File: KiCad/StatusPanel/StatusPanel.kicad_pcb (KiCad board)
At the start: 2 copper layers, 95 x 85 mm, 17 parts, among them U1 CC56-12EWA

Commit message: ステータスパネルの3Dモデルを生成
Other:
- board text removed: "N2O"
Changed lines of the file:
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@@
       (stroke (width 0.05) (type solid)) (fill none) (layer "F.CrtYd"))
     (pad "" np_thru_hole circle (at 0 0) (size 7 7) (drill 7) (layers "F&B.Cu" "*.Mask"))
+    (model "${KIPRJMOD}/LED_Bracket_Red.step"
+      (offset (xyz 0 0 0))
+      (scale (xyz 1 1 1))
+      (rotate (xyz 0 0 0))
+    )
   )
   (footprint "MountingHole:MountingHole_4.5mm" (layer "F.Cu")
@@
       (stroke (width 0.05) (type solid)) (fill none) (layer "F.CrtYd"))
     (pad "" np_thru_hole circle (at 0 0) (size 7 7) (drill 7) (layers "*.Cu" "*.Mask"))
+    (model "${KIPRJMOD}/LED_Bracket_Red.step"
+      (offset (xyz 0 0 0))
+      (scale (xyz 1 1 1))
+      (rotate (xyz 0 0 0))
+    )
   )
   (footprint "MountingHole:MountingHole_4.5mm" (layer "F.Cu")
@@
       (stroke (width 0.05) (type solid)) (fill none) (layer "F.CrtYd"))
     (pad "" np_thru_hole circle (at 0 0) (size 7 7) (drill 7) (layers "*.Cu" "*.Mask"))
+    (model "${KIPRJMOD}/LED_Bracket_Green.step"
+      (offset (xyz 0 0 0))
+      (scale (xyz 1 1 1))
+      (rotate (xyz 0 0 0))
+    )
   )
   (footprint "MountingHole:MountingHole_6mm" (layer "F.Cu")
@@
       (stroke (width 0.05) (type solid)) (fill none) (layer "F.CrtYd"))
     (pad "" np_thru_hole circle (at 0 0) (size 7 7) (drill 7) (layers "*.Cu" "*.Mask"))
+    (model "${KIPRJMOD}/LED_Bracket_Orange.step"
+      (offset (xyz 0 0 0))
+      (scale (xyz 1 1 1))
+      (rotate (xyz 0 0 0))
+    )
   )
   (footprint "MountingHole:MountingHole_6mm" (layer "F.Cu")
@@
       (stroke (width 0.05) (type solid)) (fill none) (layer "F.CrtYd"))
     (pad "" np_thru_hole circle (at 0 0) (size 22 22) (drill 22) (layers "F&B.Cu" "*.Mask"))
+    (model "${KIPRJMOD}/USB.step"
+      (offset (xyz 0 0 0))
+      (scale (xyz 1 1 1))
+      (rotate (xyz 0 0 0))
+    )
   )
   (footprint "MountingHole:MountingHole_6mm" (layer "F.Cu")
@@
       (stroke (width 0.05) (type solid)) (fill none) (layer "F.CrtYd"))
     (pad "" np_thru_hole circle (at 0 0) (size 7 7) (drill 7) (layers "*.Cu" "*.Mask"))
+    (model "${KIPRJMOD}/LED_Bracket_Green.step"
+      (offset (xyz 0 0 0))
+      (scale (xyz 1 1 1))
+      (rotate (xyz 0 0 0))
+    )
   )
   (footprint "MountingHole:MountingHole_4.5mm" (layer "F.Cu")
@@
       (stroke (width 0.05) (type solid)) (fill none) (layer "F.CrtYd"))
     (pad "" np_thru_hole circle (at 0 0) (size 7 7) (drill 7) (layers "*.Cu" "*.Mask"))
+    (model "${KIPRJMOD}/LED_Bracket_Orange.step"
+      (offset (xyz 0 0 0))
+      (scale (xyz 1 1 1))
+      (rotate (xyz 0 0 0))
+    )
   )
   (footprint "MountingHole:MountingHole_6mm" (layer "F.Cu")
@@
       (stroke (width 0.05) (type solid)) (fill none) (layer "F.CrtYd"))
     (pad "" np_thru_hole circle (at 0 0) (size 7 7) (drill 7) (layers "*.Cu" "*.Mask"))
+    (model "${KIPRJMOD}/LED_Bracket_Blue.step"
+      (offset (xyz 0 0 0))
+      (scale (xyz 1 1 1))
+      (rotate (xyz 0 0 0))
+    )
   )
   (footprint "MountingHole:MountingHole_4.5mm" (layer "F.Cu")
@@
       (stroke (width 0.05) (type solid)) (fill none) (layer "F.CrtYd"))
     (pad "" np_thru_hole circle (at 0 0) (size 13.77 13.77) (drill 13.77) (layers "F&B.Cu" "*.Mask"))
+    (model "${KIPRJMOD}/Button.step"
+      (offset (xyz 0 0 0))
+      (scale (xyz 1 1 1))
+      (rotate (xyz 0 0 0))
+    )
   )
   (footprint "MountingHole:MountingHole_4.5mm" (layer "F.Cu")
@@
       (stroke (width 0.05) (type solid)) (fill none) (layer "F.CrtYd"))
     (pad "" np_thru_hole circle (at 0 0) (size 7 7) (drill 7) (layers "*.Cu" "*.Mask"))
+    (model "${KIPRJMOD}/LED_Bracket_Blue.step"
+      (offset (xyz 0 0 0))
+      (scale (xyz 1 1 1))
+      (rotate (xyz 0 0 0))
+    )
   )
   (footprint "Display_7Segment:CA56-12CGKWA" (layer "F.Cu")
@@
     (effects (font (size 2 2) (thickness 0.3)) (justify top))
   )
-  (gr_text "N2O" (at 123.85 58.9) (layer "F.SilkS")
-    (effects (font (size 3 3) (thickness 0.3)) (justify left))
-  )
   (gr_text "SYSTEM" (at 85.85 91.9) (layer "F.SilkS")
     (effects (font (size 2 2) (thickness 0.3)))
@@
     (effects (font (size 2 2) (thickness 0.3)) (justify top))
   )
-  (gr_text "MPa" (at 122.85 66.9) (layer "F.SilkS")
-    (effects (font (size 7 7) (thickness 0.5)) (justify left))
+  (gr_text "MPa" (at 121.85 63.9) (layer "F.SilkS")
+    (effects (font (size 7 7) (thickness 0.7)) (justify left))
   )
   (gr_text "RESET" (at 104.85 116.9) (layer "F.SilkS")

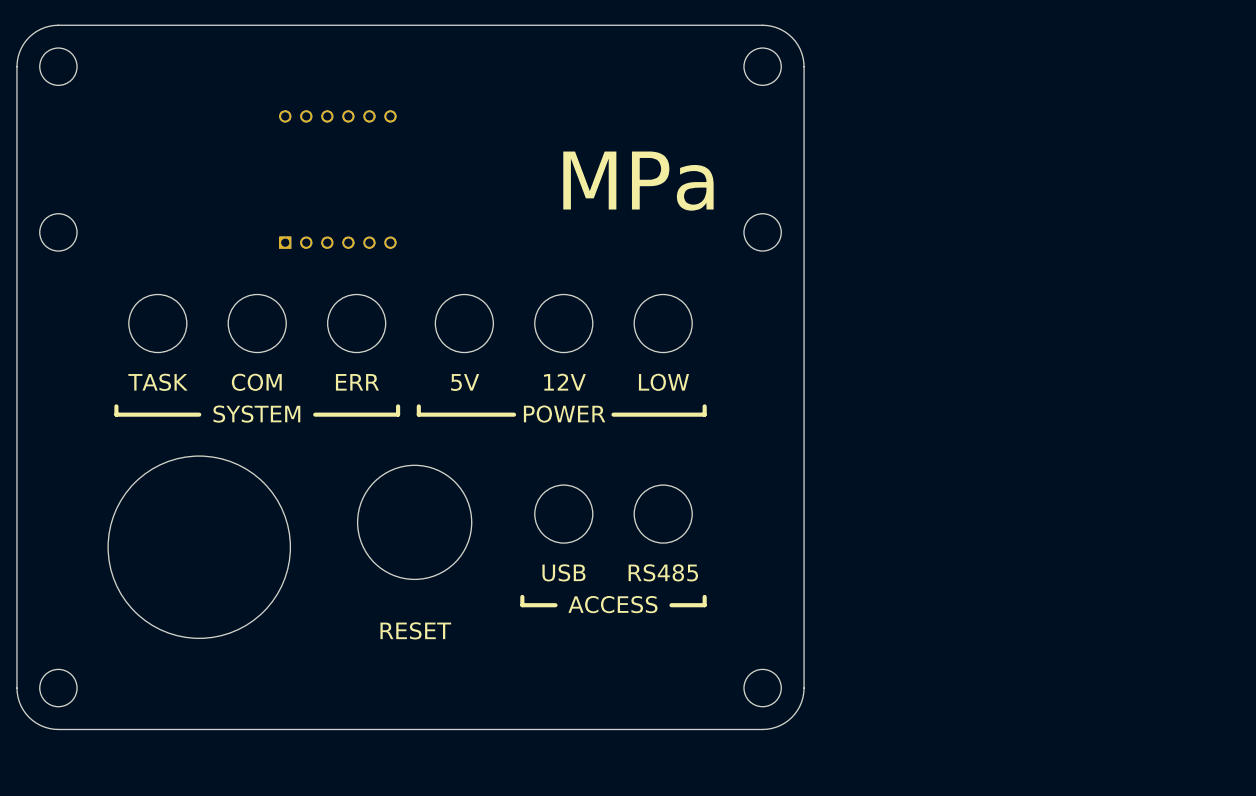
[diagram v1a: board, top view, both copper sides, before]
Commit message: ステータスパネルを再設計
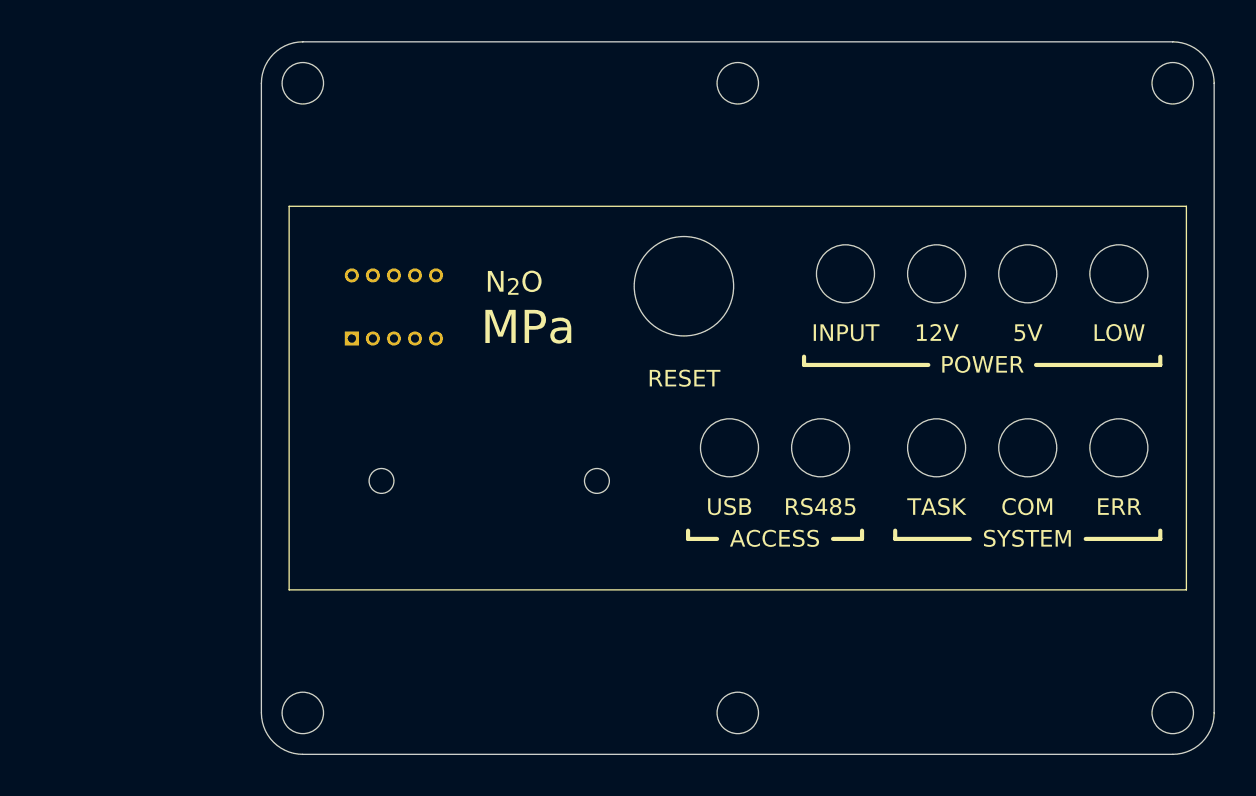
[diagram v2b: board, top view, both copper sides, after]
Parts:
- removed the REF** at (146.8, 69.9)
- removed the REF** at (61.9, 124.9)
- removed the REF** at (61.9, 49.9)
- removed the REF** at (146.8, 49.9)
- removed the REF** at (146.8, 124.9)
- removed the REF** at (61.9, 69.9)
- removed U1: CC56-12EWA, Display_7Segment:CA56-12CGKWA
- added REF**: MountingHole_5mm, MountingHole:MountingHole_5mm, F.Cu at (91.3, 51.9)
- added REF**: MountingHole_6mm, MountingHole:MountingHole_6mm, F.Cu at (156.8, 74.9)
- added REF**: MountingHole_5mm, MountingHole:MountingHole_5mm, F.Cu at (143.8, 127.9)
- added REF**: MountingHole_5mm, MountingHole:MountingHole_5mm, F.Cu at (143.8, 51.9)
- added REF**: MountingHole_5mm, MountingHole:MountingHole_5mm, F.Cu at (91.3, 127.9)
- added REF**: MountingHole_5mm, MountingHole:MountingHole_5mm, F.Cu at (196.3, 51.9)
- added REF**: Sx39-1xxxxx, Display_7Segment:Sx39-1xxxxx, F.Cu at (97.3, 82.7)
- added REF**: MountingHole_5mm, MountingHole:MountingHole_5mm, F.Cu at (196.3, 127.9)
- moved REF** 95.2 mm to (167.8, 95.9)
- moved REF** 94.2 mm to (178.8, 95.9)
- moved REF** 93.2 mm to (189.8, 95.9)
- moved REF** 57.3 mm to (167.8, 74.9)
- moved REF** 56.3 mm to (178.8, 74.9)
- moved REF** 55.3 mm to (189.8, 74.9)
- moved REF** 43.2 mm to (137.3, 76.4)
- moved REF** 35.9 mm to (113.8, 99.9)
- moved REF** 21.5 mm to (142.8, 95.9)
- moved REF** 20.6 mm to (153.8, 95.9)
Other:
- board size 95 x 85 mm -> 115 x 86 mm
- board text added: "INPUT"
- board text added: "N_{2}O"
- board text removed: "LaunchController"
- board text removed: "SatelliteController"

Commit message: ステータスパネルの裏面に配線を追加
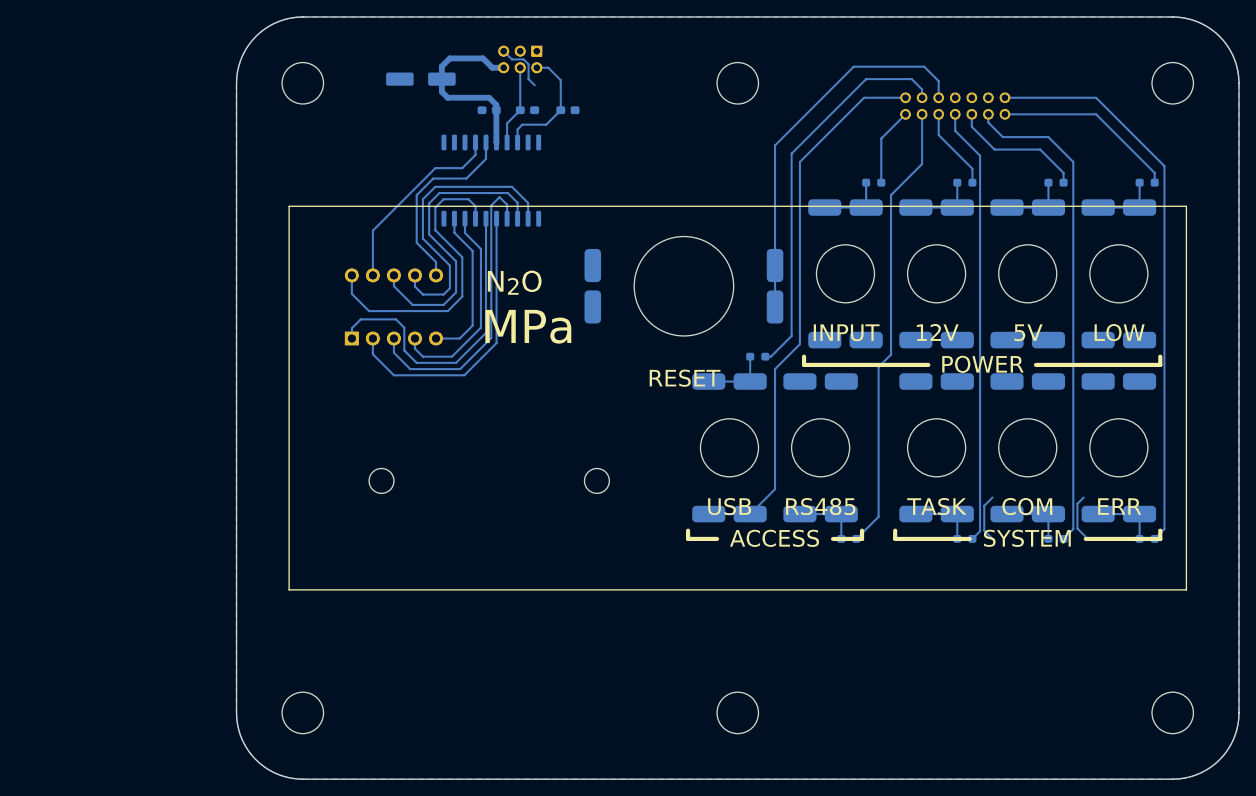
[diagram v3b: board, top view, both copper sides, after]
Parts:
- removed the REF** at (97.3, 82.7)
- added C1: 0.1uF, Capacitor_SMD:C_0603_1608Metric_Pad1.08x0.95mm_HandSolder, B.Cu at (113.8, 55.1)
- added C2: 0.1uF, Capacitor_SMD:C_0603_1608Metric_Pad1.08x0.95mm_HandSolder, B.Cu at (123.3, 55.1)
- added C3: 0.1uF, Capacitor_SMD:C_0603_1608Metric_Pad1.08x0.95mm_HandSolder, B.Cu at (118.5, 55.1)
- added C4: 100uF, Capacitor_SMD:C_Elec_6.3x7.7, B.Cu at (105.6, 51.4)
- added J1: CONN, TSRP_Connector_Hirose:DF51A-14DP-2DS, B.Cu at (164.1, 55.6)
- added J10: CONN_12V_CTL, TSRP_Connector_Generic:1p, B.Cu at (167.8, 66.9)
- added J11: CONN_12V_GND, TSRP_Connector_Generic:1p, B.Cu at (167.8, 82.9)
- added J12: CONN_TASK_CTL, TSRP_Connector_Generic:1p, B.Cu at (167.8, 103.9)
- added J13: CONN_TASK_GND, TSRP_Connector_Generic:1p, B.Cu at (167.8, 87.9)
- added J14: CONN_5V_CTL, TSRP_Connector_Generic:1p, B.Cu at (178.8, 66.9)
- added J15: CONN_5V_GND, TSRP_Connector_Generic:1p, B.Cu at (178.8, 82.9)
- added J16: CONN_COM_CTL, TSRP_Connector_Generic:1p, B.Cu at (178.8, 103.9)
- added J17: CONN_COM_GND, TSRP_Connector_Generic:1p, B.Cu at (178.8, 87.9)
- added J18: CONN_LOW_CTL, TSRP_Connector_Generic:1p, B.Cu at (189.8, 66.9)
- added J19: CONN_LOW_GND, TSRP_Connector_Generic:1p, B.Cu at (189.8, 82.9)
- added J2: CONN_RESET_CTL, TSRP_Connector_Generic:1p, B.Cu at (148.3, 76.4)
- added J20: CONN_ERROR_CTL, TSRP_Connector_Generic:1p, B.Cu at (189.8, 103.9)
- added J21: CONN_ERROR_GND, TSRP_Connector_Generic:1p, B.Cu at (189.8, 87.9)
- added J22: CONN_7SEG, TSRP_Connector_Hirose:DF51A-6DP-2DSA, B.Cu at (117.6, 49.0)
- added J3: CONN_RESET_GND, TSRP_Connector_Generic:1p, B.Cu at (126.3, 76.4)
- added J4: CONN_USB_5V, TSRP_Connector_Generic:1p, B.Cu at (142.8, 103.9)
- added J5: CONN_USB_CTL, TSRP_Connector_Generic:1p, B.Cu at (142.8, 87.9)
- added J6: CONN_INPUT_CTL, TSRP_Connector_Generic:1p, B.Cu at (156.8, 66.9)
- added J7: CONN_INPUT_GND, TSRP_Connector_Generic:1p, B.Cu at (156.8, 82.9)
- added J8: CONN_RS485_CTL, TSRP_Connector_Generic:1p, B.Cu at (153.8, 103.9)
- added J9: CONN_RS485_GND, TSRP_Connector_Generic:1p, B.Cu at (153.8, 87.9)
- added R1: R, Resistor_SMD:R_0603_1608Metric_Pad0.98x0.95mm_HandSolder, B.Cu at (146.3, 84.9)
- added R2: R, Resistor_SMD:R_0603_1608Metric_Pad0.98x0.95mm_HandSolder, B.Cu at (160.3, 63.9)
- added R3: R, Resistor_SMD:R_0603_1608Metric_Pad0.98x0.95mm_HandSolder, B.Cu at (157.3, 106.9)
- added R4: R, Resistor_SMD:R_0603_1608Metric_Pad0.98x0.95mm_HandSolder, B.Cu at (171.3, 63.9)
- added R5: R, Resistor_SMD:R_0603_1608Metric_Pad0.98x0.95mm_HandSolder, B.Cu at (171.3, 106.9)
- added R6: R, Resistor_SMD:R_0603_1608Metric_Pad0.98x0.95mm_HandSolder, B.Cu at (182.3, 63.9)
- added R7: R, Resistor_SMD:R_0603_1608Metric_Pad0.98x0.95mm_HandSolder, B.Cu at (182.3, 106.9)
- added R8: R, Resistor_SMD:R_0603_1608Metric_Pad0.98x0.95mm_HandSolder, B.Cu at (193.3, 63.9)
- added R9: R, Resistor_SMD:R_0603_1608Metric_Pad0.98x0.95mm_HandSolder, B.Cu at (193.3, 106.9)
- added U1: 2281SB, Display_7Segment:Sx39-1xxxxx, F.Cu at (97.3, 82.7)
- added U2: TM1637, Package_SO:SOP-20_7.5x12.8mm_P1.27mm, B.Cu at (114.1, 63.6)
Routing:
- net ERROR: track 0.00 -> 68.2 mm
- net +5V: track 0.00 -> 65.9 mm
- net COM: track 0.00 -> 59.2 mm
- net RS485: track 0.00 -> 54.5 mm
- net TASK: track 0.00 -> 52.9 mm
- net USB: track 0.00 -> 47.2 mm
- net RESET: track 0.00 -> 45.9 mm
- net Net-(U1-E): track 0.00 -> 36.9 mm
- net Net-(U1-F): track 0.00 -> 36.4 mm
- net Net-(U1-C): track 0.00 -> 36.2 mm
- net Net-(U1-B): track 0.00 -> 36.1 mm
- net Net-(U1-D): track 0.00 -> 34.5 mm
- net Net-(U1-A): track 0.00 -> 34.4 mm
- net Net-(U1-G): track 0.00 -> 25.0 mm
- net +5VP: track 0.00 -> 23.2 mm
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- added copper zone on B.Cu, net GND
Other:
- board size 115 x 86 mm -> 121 x 92 mm

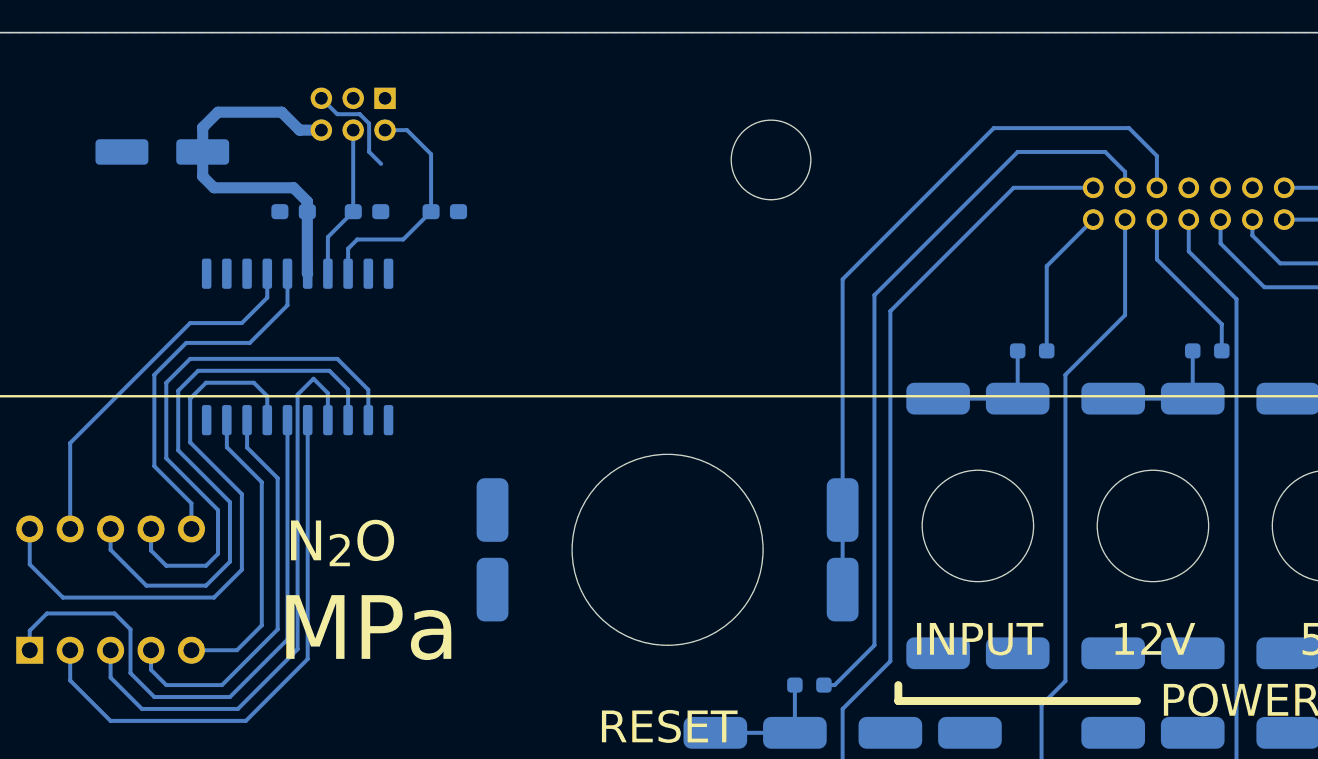
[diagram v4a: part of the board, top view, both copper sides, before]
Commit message: 7セグ用コネクタを6Pから14Pの空いているピンに押し込んだ
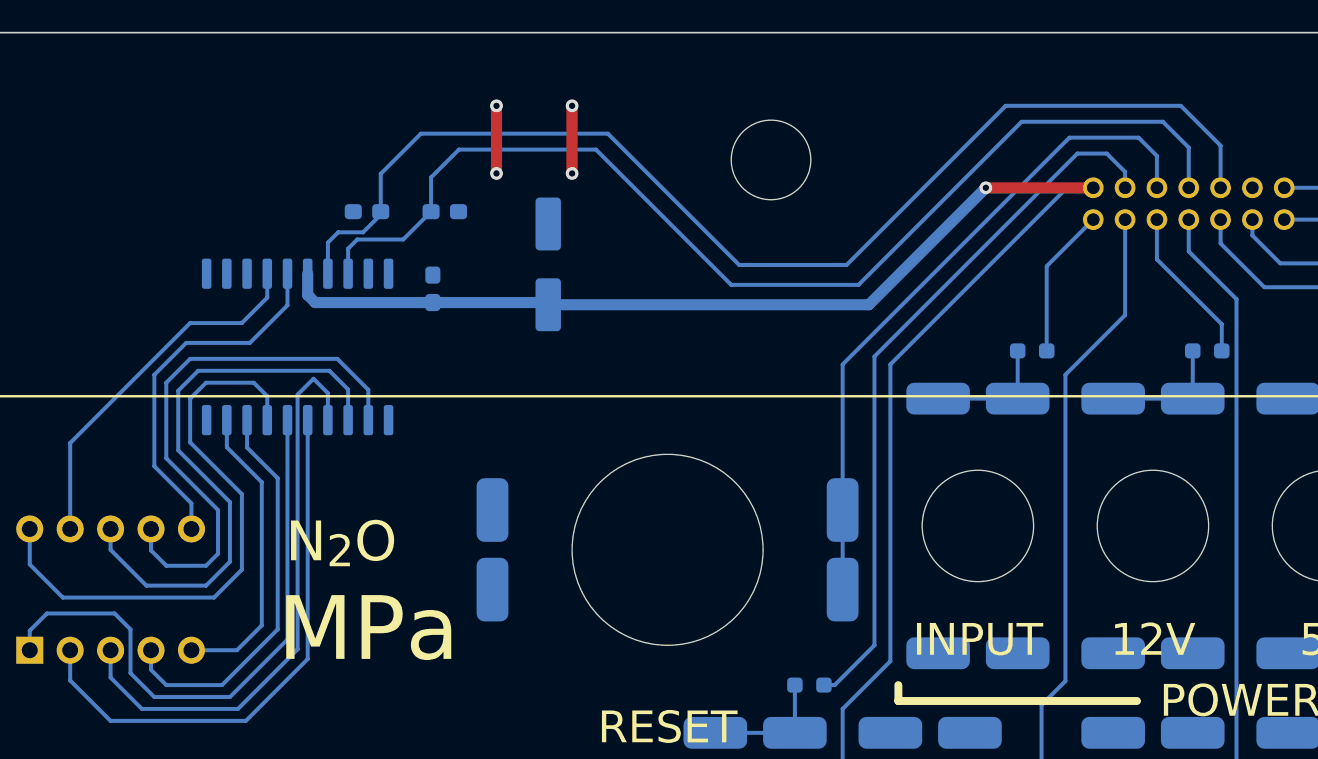
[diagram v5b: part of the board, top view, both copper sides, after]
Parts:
- removed J22: CONN_7SEG, TSRP_Connector_Hirose:DF51A-6DP-2DSA
- R1, R2, R3, R4, R5, R6, R7, R8, R9: value R -> 270R
- moved C4 25.3 mm to (129.8, 58.5), turned to 90 degrees
- moved C1 10.0 mm to (122.6, 60.0), turned to -90 degrees
- turned C3 to 0 degrees
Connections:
- C1 pad 2: +5VP -> +5V
- C4 pad 1: +5VP -> +5V
- J1 pad 10: unconnected-(J1-Pin_10-Pad10) -> DIO
- J1 pad 8: unconnected-(J1-Pin_8-Pad8) -> CLK
- U2 pad 16: +5VP -> +5V
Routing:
- net DIO: track 9.68 -> 73.6 mm
- net CLK: track 14.9 -> 69.2 mm
- net +5V: track 65.9 -> 118.1 mm, vias 0 -> 1
- net +5VP: track 23.2 -> 0.00 mm
- net RESET: track 45.9 -> 42.3 mm
- net USB: track 47.2 -> 44.9 mm
- net GND: track 18.2 -> 20.2 mm, vias 0 -> 4
